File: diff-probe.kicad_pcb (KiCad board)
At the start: 4 copper layers, 67 x 16 mm, 40 parts, among them J1 Conn_01x02, J2 73100-0167 (BNC), J3 Conn_01x03, U1 LTC6228xS8, U2 LTC6228xS8, U3 LTC6228xS8

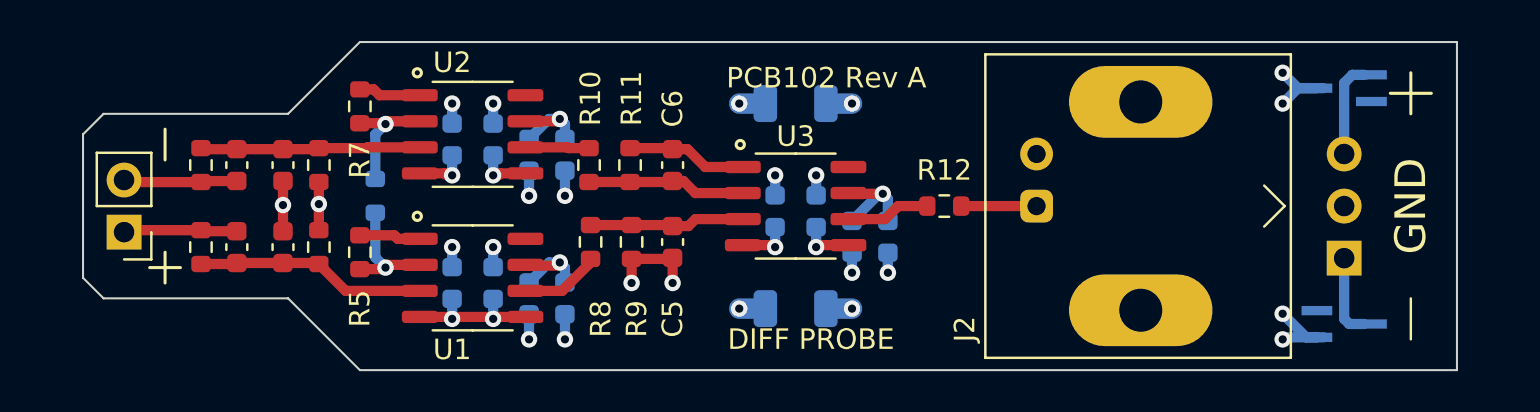
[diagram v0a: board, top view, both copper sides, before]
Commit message: Added LEDs and moutning holes. Generated PDF drawing and gerbers.
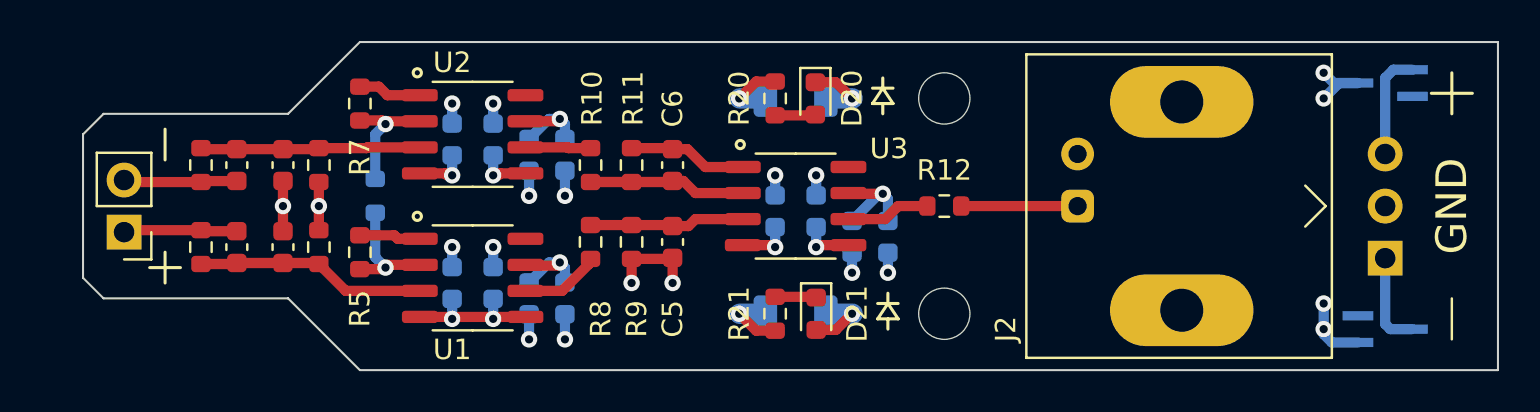
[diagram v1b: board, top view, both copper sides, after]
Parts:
- removed D3, D4: BAT54W, Package_TO_SOT_SMD:SOT-323_SC-70_Handsoldering
- added D1: BAT54W, Package_TO_SOT_SMD:SOT-323_SC-70_Handsoldering, B.Cu at (96.5, 44.0)
- added D2: BAT54W, Package_TO_SOT_SMD:SOT-323_SC-70_Handsoldering, B.Cu at (96.5, 56.0)
- added D20: LED, Diode_SMD:D_0603_1608Metric, F.Cu at (68.7, 44.8)
- added D21: LED, Diode_SMD:D_0603_1608Metric, F.Cu at (68.8, 55.2)
- added H1: MountingHole, MountingHole:MountingHole_2.5mm, F.Cu at (75.0, 44.8)
- added H2: MountingHole, MountingHole:MountingHole_2.5mm, F.Cu at (75.0, 55.2)
- added R20: 698, Resistor_SMD:R_0603_1608Metric, F.Cu at (66.8, 44.8)
- added R21: 698, Resistor_SMD:R_0603_1608Metric, F.Cu at (66.8, 55.2)
- C2, C4: value 56pF -> 68pF
- J2: value 73100-0167 (BNC) -> 73100-0167
- U1, U2, U3: value LTC6228xS8 -> LTC6228HS8
- moved J2 2.00 mm to (81.5, 50.0)
- moved J3 2.00 mm to (96.5, 52.5)
- moved C40 0.25 mm to (67.8, 44.8), turned to 0 degrees
- moved C41 0.25 mm to (67.8, 55.2), turned to 180 degrees
- moved R7 0.13 mm to (46.5, 45.0)
- moved R10 0.08 mm to (57.8, 48.0)
- moved R11 0.08 mm to (59.8, 48.0)
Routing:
- net GND: track 24.1 -> 28.3 mm
- net Net-(D21-Pad1): track 0.00 -> 2.02 mm
- net /OUT: track 3.67 -> 5.67 mm
- net Net-(D20-Pad2): track 0.00 -> 1.98 mm
- net VDD: track 20.0 -> 21.6 mm
- net VSS: track 22.6 -> 23.5 mm
- net /POS: track 4.63 -> 5.21 mm
- net /NEG: track 4.06 -> 4.64 mm
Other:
- board size 67 x 16 mm -> 69 x 16 mm
- board text added: "THE PRODUCT IS PROVIDED {dblquote}AS IS{dblquote}, WITHOUT WARRANTY OF ANY KIND, EXPRESS OR IMPLIED, INCLUDING BUT NOT LIMITED TO THE WARRANTIES OF MERCHANTABILITY, FITNESS FOR A PARTICULAR PURPOSE AND NONINFRINGEMENT. IN NO EVENT SHALL THE AUTHORS OR COPYRIGHT HOLDERS BE LIABLE FOR ANY CLAIM, DAMAGES OR OTHER LIABILITY, WHETHER IN AN ACTION OF CONTRACT, TORT OR OTHERWISE, ARISING FROM, OUT OF OR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"

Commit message: Miscellaneous cleanup
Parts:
- moved C30 0.56 mm to (72.5, 51.0)
- moved C32 0.56 mm to (70.8, 51.0)
- moved C10 0.25 mm to (56.8, 54.5)
- moved C12 0.25 mm to (55.0, 54.5)
- moved C20 0.25 mm to (56.8, 47.5)
- moved C22 0.25 mm to (55.0, 47.5)
- moved R5 0.25 mm to (46.5, 52.0)
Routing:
- net VDD: track 21.6 -> 20.8 mm
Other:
- outline, holes or cut-outs redrawn

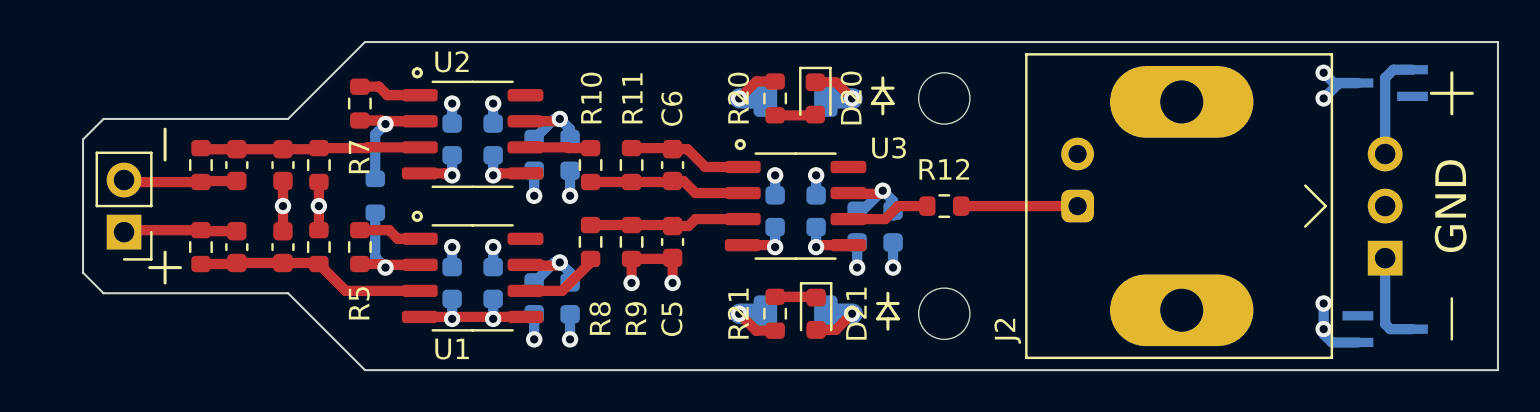
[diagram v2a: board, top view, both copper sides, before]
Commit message: Update component values
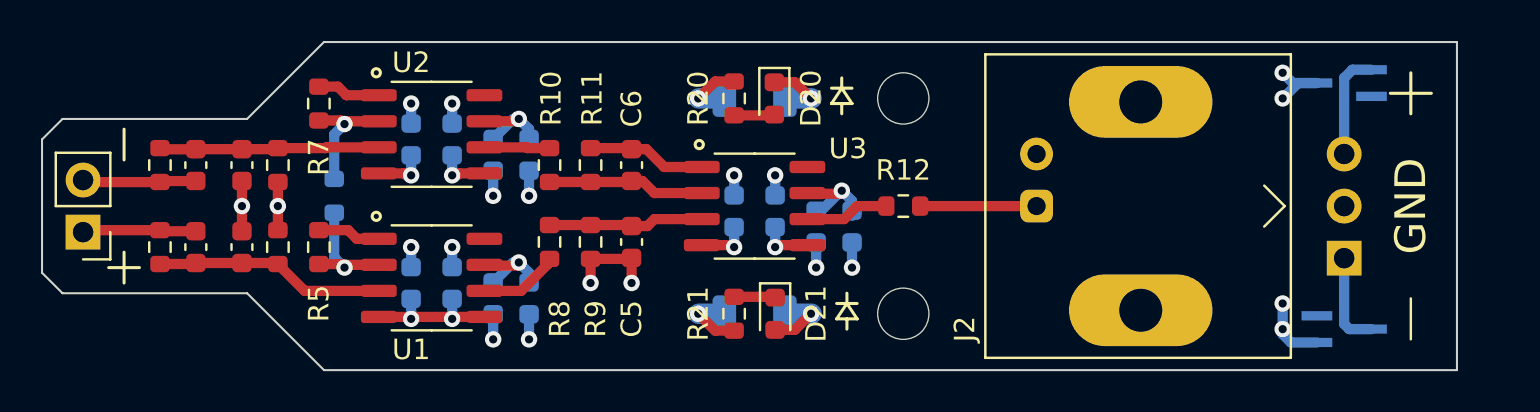
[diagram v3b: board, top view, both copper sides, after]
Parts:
- moved C1 2.00 mm to (38.5, 52.0)
- moved C10 2.00 mm to (54.8, 54.5)
- moved C11 2.00 mm to (51.0, 53.8)
- moved C12 2.00 mm to (53.0, 54.5)
- moved C13 2.00 mm to (49.0, 53.8)
- moved C2 2.00 mm to (40.8, 52.0)
- moved C20 2.00 mm to (54.8, 47.5)
- moved C21 2.00 mm to (51.0, 46.8)
- moved C22 2.00 mm to (53.0, 47.5)
- moved C23 2.00 mm to (49.0, 46.8)
- moved C3 2.00 mm to (38.5, 48.0)
- moved C30 2.00 mm to (70.5, 51.0)
- moved C31 2.00 mm to (66.8, 50.2)
- moved C32 2.00 mm to (68.8, 51.0)
- moved C33 2.00 mm to (64.8, 50.2)
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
